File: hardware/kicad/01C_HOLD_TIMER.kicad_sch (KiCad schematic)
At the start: 13 parts, among them U501 TLC555QDRQ1 - MONOSTABLE 24s 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, U502 SN74LVC1G08-Q1 AND

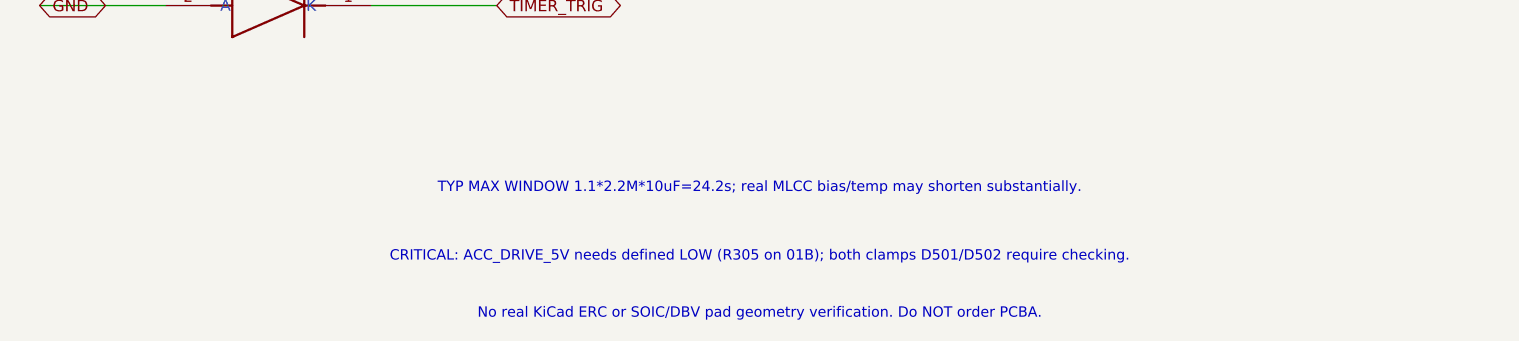
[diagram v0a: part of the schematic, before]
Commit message: docs(schematic): remove stale relay and absent-R305 references from active 555 timer annotations
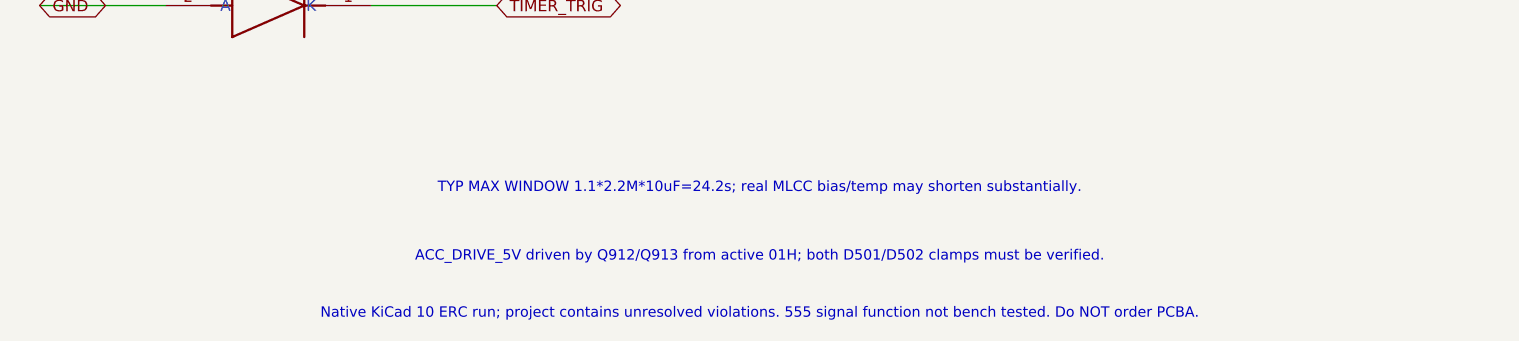
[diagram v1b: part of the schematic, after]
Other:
- note added: "ACC_DRIVE_5V driven by Q912/Q913 from active 01H; both D501/D502 clamps must be verified."
- note added: "Native KiCad 10 ERC run; project contains unresolved violations. 555 signal function not bench tested. Do NOT order PCBA."
- note removed: "CRITICAL: ACC_DRIVE_5V needs defined LOW (R305 on 01B); both clamps D501/D502 require checking."
- note removed: "No real KiCad ERC or SOIC/DBV pad geometry verification. Do NOT order PCBA."
- title: TripTracer V1 - Hardware-Timer / RELAY_HOLD -> TripTracer V1 - ACC OFF MCU HOLD timer
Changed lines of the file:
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@@
 (kicad_sch (version 20250114) (generator "eeschema")
 (paper "A3")
-(title_block (title "TripTracer V1 - Hardware-Timer / RELAY_HOLD") (date "2026-10-13") (rev "a3 / PROVISIONAL / ERC NOT RUN"))
+(title_block (title "TripTracer V1 - ACC OFF MCU HOLD timer") (date "2026-10-13") (rev "b0 / GRID REPAIRED / ERC NOT CLEAN"))
 (symbol (lib_id "TripTracer_V1:TLC555_Q1") (at 170.18 110.49 0) (unit 1) (exclude_from_sim no) (in_bom yes) (on_board yes) (dnp no)
 (property "Reference" "U501" (at 170.18 91.44 0) (effects (font (size 1.27 1.27))))
@@
 (text "MCU_HOLD_REQ must be active WHILE ACC is high; goes low immediately after SD unmount." (at 204.47 59.69 0) (effects (font (size 1.15 1.15))))
 (text "TYP MAX WINDOW 1.1*2.2M*10uF=24.2s; real MLCC bias/temp may shorten substantially." (at 204.47 276.86 0) (effects (font (size 1.15 1.15))))
-(text "CRITICAL: ACC_DRIVE_5V needs defined LOW (R305 on 01B); both clamps D501/D502 require checking." (at 204.47 284.48 0) (effects (font (size 1.15 1.15))))
-(text "No real KiCad ERC or SOIC/DBV pad geometry verification. Do NOT order PCBA." (at 204.47 290.83 0) (effects (font (size 1.15 1.15))))
+(text "ACC_DRIVE_5V driven by Q912/Q913 from active 01H; both D501/D502 clamps must be verified." (at 204.47 284.48 0) (effects (font (size 1.15 1.15))))
+(text "Native KiCad 10 ERC run; project contains unresolved violations. 555 signal function not bench tested. Do NOT order PCBA." (at 204.47 290.83 0) (effects (font (size 1.15 1.15))))
 (sheet_instances (path "/a26d9b0c-7f10-4e5a-a65f-000000000064/a26d9b0c-7f10-4e5a-a65f-000000000065" (page "2.3")))
 (embedded_fonts no)

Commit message: fix(power): prearm timed HOLD before ACC falls and protect inverse-ACC sensing
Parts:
- removed C502: 10nF AC falling-edge pulse, Tripmaster:C_1206_3216, symbol Tripmaster_Sym:C
- removed D501: BAT54WS TRIG positive clamp, Tripmaster:D_BAT54WS_SOD323, symbol Tripmaster_Sym:SCHOTTKY
- removed D502: BAT54WS TRIG negative clamp, Tripmaster:D_BAT54WS_SOD323, symbol Tripmaster_Sym:SCHOTTKY
- added D503: BAS116Q-7-F LOW LEAK, Package_TO_SOT_SMD:SOT-23, symbol TripTracer_V1:BAS116Q_SOT23
- added R505: 10k 1% RC discharge limit, Tripmaster:R_1206_3216, symbol Tripmaster_Sym:R
- C501: value 10uF 16V X7R (1210), DERATE -> 22uF 25V X7R 1210 DERATE; MPN (none) -> GRM32ER71E226KE15L
- R501: value 2.2M 1% - tMAX -> 1M 1% - OFF DEADLINE; MPN (none) -> ERJP08F1004V
- U501: value TLC555QDRQ1 - MONOSTABLE 24s NOM -> TLC555QDRQ1 - PREARMED OFF TIMER
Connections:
- net TIMER_RC: now also R505.1
- net TIMER_TRIG renamed ACC_INV_N
- net ACC_INV_N: now also D503.3 (K3)
- new net TIMER_RC_CLAMP: D503.1 (A1), R505.2
- no-connect marks 0 -> 1
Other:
- note added: "01C PREARMED ACC-OFF TIMER - SUBCIRCUIT, NOT SYSTEM-VALIDATED"
- note added: "1M / 22uF retain 22s nominal RC product with more leakage margin; actual window depends on clamp, bias and thresholds."
- note added: "ACC OFF: TRIG rises, RC charges; OUT retains HIGH until timeout. U502 AND MCU_HOLD_REQ permits early release."
- note added: "ACC ON: Q912 holds TRIG low and discharges RC via D503/R505; HOLD is already armed before ACC falls."
- note added: "ACC_INV_N is global from Q912; D503 K3=ACC_INV_N, A1=RC via 10k, NC2. C502 and its D501/D502 clamps removed."
- note removed: "01C MONOSTABLE HARDWARE HOLD WINDOW - SUBCIRCUIT, NOT SYSTEM-VALIDATED"
- note removed: "ACC_DRIVE_5V driven by Q912/Q913 from active 01H; both D501/D502 clamps must be verified."
- note removed: "ACC_DRIVE_5V falls -> C502/R502 generates a SHORT LOW TRIG pulse; TRIG must RETURN HIGH."
- note removed: "TYP MAX WINDOW 1.1*2.2M*10uF=24.2s; real MLCC bias/temp may shorten substantially."
- note removed: "Timer OUT high only during window; U502 output = timer_window AND MCU_HOLD_REQ."
